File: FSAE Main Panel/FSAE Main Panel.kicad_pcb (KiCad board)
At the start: 2 copper layers, 175 x 58.5 mm, 150 parts, among them J201 USB Micro B, J202 Cortex_Debug, J203 Conn_01x04, J204 TE_84953-6_FPC, Q301 IRLML6402TRPBF, Q501 SI2308CDS-T1-GE3, Q502 SI2308CDS-T1-GE3, SW1 B3W-1020, SW2 B3W-1020, U1 SAMD21G18A-AU, U301 UA7805CKTTR, U302 LP2985-3.3, U303 LM1085-5.0, U304 UA7805CKTTR, U401 MCP2515-I/ST, U402 MCP2551-I/SN, U501 TLC6C598, U502 TLC6C5816, U503 TLC6C5816, U504 TLC6C5816, Y101 32.768kHz, Y401 Resonator

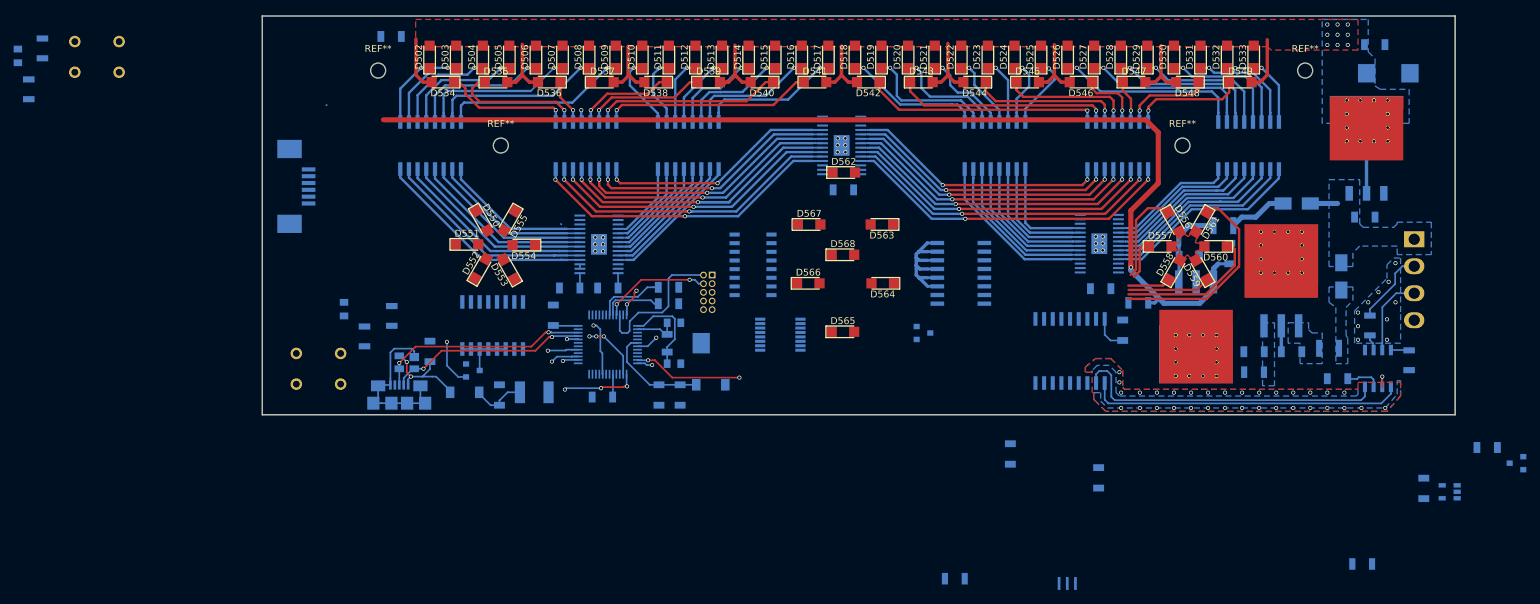
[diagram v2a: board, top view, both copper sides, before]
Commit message: Power Supply Changes Again
Shrunk some 5V layout by switching LM7805's for their SOT223 packages but with very careful top copper considerations for thermal management.
Shrunk the Right side by 12mm for more clearance near ignition button.
Fixed Shift Register clock signal routing.
Changed shift order to be 7 segment first for easiler routing.
Added Mounting Holes.
TODO: Figure out Top layer 7 segment placement.
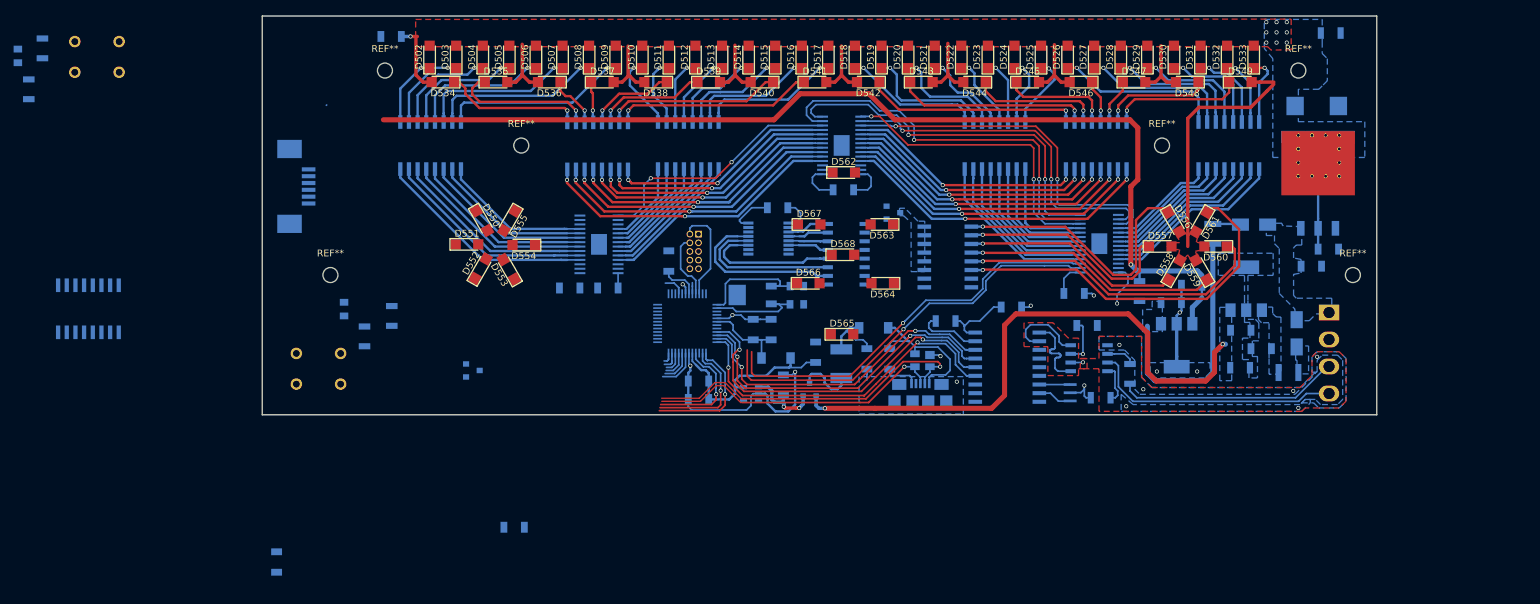
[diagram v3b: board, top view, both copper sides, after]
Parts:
- added REF**: MountingHole_2.2mm_M2, Mounting_Holes:MountingHole_2.2mm_M2, F.Cu at (87.5, 68.0)
- added REF**: MountingHole_2.2mm_M2, Mounting_Holes:MountingHole_2.2mm_M2, F.Cu at (237.5, 68.0)
- U301, U304: value UA7805CKTTR -> LM7805; footprint Texas_Additions:TO-263-3_TabPin2_PAD_2012 -> TO_SOT_Packages_SMD:SOT-223-3_TabPin2
- moved C305 107.2 mm to (141.5, 86.2), turned to 180 degrees
- moved Q301 104.3 mm to (157.8, 84.8), turned to 90 degrees
- moved C304 103.7 mm to (153.9, 84.2), turned to 90 degrees
- moved U302 103.5 mm to (149.2, 85.4)
- moved R302 78.0 mm to (234.2, 32.5)
- moved J201 76.5 mm to (174.1, 86.6)
- moved D201 75.7 mm to (174.3, 80.5)
- moved C203 67.5 mm to (169.6, 80.3), turned to 90 degrees
- moved L201 60.7 mm to (167.2, 75.8), turned to 0 degrees
- moved RN508 59.4 mm to (52.0, 73.0)
- moved C106 54.4 mm to (79.6, 110.1)
- moved C204 54.2 mm to (166.2, 80.3), turned to 90 degrees
- moved C502 49.7 mm to (153.1, 58.1), turned to 180 degrees
- moved R402 45.6 mm to (200.5, 86.0), turned to 180 degrees
- moved C501 45.4 mm to (158.7, 79.3), turned to 90 degrees
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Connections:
- J203 pad 2: CAN_IN- -> GND
- J203 pad 3: CAN_IN+ -> CAN_IN-
- J203 pad 4: GND -> CAN_IN+
- RN501 pad 1: /Display/aI -> /Display/a
- RN501 pad 10: /Display/g -> /Display/gI
- RN501 pad 11: /Display/f -> /Display/fI
- RN501 pad 12: /Display/e -> /Display/eI
- RN501 pad 13: /Display/d -> /Display/dI
- RN501 pad 14: /Display/c -> /Display/cI
- RN501 pad 15: /Display/b -> /Display/bI
- RN501 pad 16: /Display/a -> /Display/aI
- RN501 pad 2: /Display/bI -> /Display/b
- RN501 pad 3: /Display/cI -> /Display/c
- RN501 pad 4: /Display/dI -> /Display/d
- RN501 pad 5: /Display/eI -> /Display/e
- RN501 pad 6: /Display/fI -> /Display/f
- RN501 pad 7: /Display/gI -> /Display/g
- U1 pad 20: RPM_IN -> GEAR_IN
- U1 pad 24: RPM_SCLK -> SCLK
- U1 pad 30: GEAR_SCLK -> Net-(U1-Pad30)
- U501 pad 15: GEAR_SCLK -> SCLK
- U501 pad 9: Net-(U501-Pad9) -> GEAR_OUT
- U502 pad 12: RPM_IN -> GEAR_OUT
- U502 pad 17: RPM_SCLK -> SCLK
- U503 pad 12: Net-(U502-Pad15) -> Net-(U503-Pad12)
- U503 pad 17: RPM_SCLK -> SCLK
- U504 pad 12: Net-(U503-Pad15) -> Net-(U502-Pad15)
- U504 pad 15: GEAR_IN -> Net-(U503-Pad12)
- U504 pad 17: RPM_SCLK -> SCLK
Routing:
- net +5V: track 0.00 -> 96.1 mm, vias 0 -> 4
- net GND: track 33.6 -> 96.3 mm, vias 43 -> 20
- net RPM_CLR: track 0.00 -> 61.6 mm, vias 0 -> 2
- net /Display/~G3: track 0.00 -> 60.8 mm, vias 0 -> 1
- net /Display/~G4: track 0.00 -> 59.3 mm, vias 0 -> 1
- net ~RPM_EN: track 0.00 -> 59.0 mm, vias 0 -> 2
- net RPM_RCLK: track 0.00 -> 55.3 mm, vias 0 -> 2
- net SCLK: track 0.00 -> 55.1 mm, vias 0 -> 2
- net CAN_MOSI: track 0.00 -> 52.2 mm, vias 0 -> 2
- net CAN_MISO: track 0.00 -> 49.2 mm, vias 0 -> 2
- net CAN_SCLK: track 2.25 -> 50.5 mm, vias 1 -> 2
- net Net-(U503-Pad12): track 0.00 -> 44.3 mm, vias 0 -> 2
- net Net-(U502-Pad15): track 0.00 -> 37.2 mm, vias 0 -> 2
- net +3V3: track 28.5 -> 65.1 mm, vias 0 -> 1
- net /CAN/CAN_TX+: track 46.3 -> 12.0 mm
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- added copper zone on B.Cu, net /Display/OP_CONTROL
- added copper zone on B.Cu, net /Power/REG2_VIN
- removed copper zone on F.Cu, net DWC_+5V
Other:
- board size 175 x 58.5 mm -> 163.5 x 58.5 mm
- board text removed: "Maximum length 160mm"
- board text removed: "Maximum width 55mm"

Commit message: Minor Routing changes
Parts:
- moved SW2 6.52 mm to (89.0, 84.5)
- moved C504 4.72 mm to (123.5, 70.3)
- moved C503 4.21 mm to (122.9, 74.1)
- moved C402 3.95 mm to (183.7, 74.0)
- moved U502 3.30 mm to (123.6, 63.5)
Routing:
- net +3V3: track 65.1 -> 116.7 mm, vias 1 -> 3
- net GND: track 96.3 -> 128.1 mm, vias 20 -> 27
- net /Display/RPM_10: track 13.2 -> 16.7 mm
- net /Display/RPM_3: track 29.6 -> 26.3 mm
- net /Display/RPM_8: track 22.1 -> 18.8 mm
- net /Display/RPM_7: track 23.4 -> 20.1 mm
- net /Display/RPM_6: track 24.9 -> 21.6 mm
- net /Display/RPM_5: track 26.5 -> 23.2 mm
- net /Display/RPM_4: track 28.0 -> 24.7 mm
- net /Display/RPM_1: track 32.6 -> 29.3 mm
- net /Display/RPM_2: track 31.1 -> 27.8 mm
- net /Display/RPM_12: track 15.9 -> 19.2 mm
- net /Display/RPM_9: track 11.9 -> 15.2 mm
- net /Display/RPM_16: track 20.8 -> 24.1 mm
- net /Display/RPM_15: track 19.5 -> 22.8 mm
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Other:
- board size 163.5 x 58.5 mm -> 157 x 58.5 mm

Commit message: More Routing
Fixed Tactile Switch Footprints
More routing
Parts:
- moved C201 69.7 mm to (103.7, 67.7), turned to 0 degrees
- moved R201 67.7 mm to (103.8, 71.0), turned to 180 degrees
- moved R202 64.2 mm to (98.2, 71.0), turned to 180 degrees
- moved C106 63.7 mm to (131.2, 72.8), turned to 270 degrees
- moved RN508 61.2 mm to (113.1, 76.7)
- moved SW1 55.3 mm to (99.5, 63.0), turned to 180 degrees
- moved C107 45.3 mm to (137.4, 65.9), turned to 90 degrees
- moved C202 14.5 mm to (103.6, 76.5), turned to 0 degrees
- moved C105 10.9 mm to (145.1, 68.8), turned to 0 degrees
- moved Q501 10.3 mm to (118.6, 83.5), turned to 180 degrees
- moved J204 10.0 mm to (90.5, 49.0)
- moved R203 7.25 mm to (103.8, 74.0), turned to 180 degrees
- moved R204 6.42 mm to (98.2, 74.0), turned to 180 degrees
- moved C104 5.74 mm to (150.2, 73.2)
- moved SW2 4.67 mm to (93.0, 82.0)
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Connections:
- C104 pad 2: /XOUT -> /XIN-
- C105 pad 2: /XIN -> /XIN+
- SW1 pad 2: /External Interface/SW1_L -> GND
- SW1 pad 3: (no net) -> /External Interface/SW1_L
- SW1 pad 4: (no net) -> /External Interface/SW1_L
- SW2 pad 2: /External Interface/SW2_L -> GND
- SW2 pad 3: (no net) -> /External Interface/SW2_L
- SW2 pad 4: (no net) -> /External Interface/SW2_L
- U1 pad 1: /XIN -> /XIN+
- U1 pad 2: /XOUT -> /XIN-
- Y101 pad 1: /XOUT -> /XIN+
- Y101 pad 2: /XIN -> /XIN-
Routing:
- net DWC_SCLK: track 18.3 -> 116.8 mm, vias 1 -> 2
- net DWC_SDI: track 19.3 -> 117.1 mm, vias 1 -> 2
- net ~CHECK_ENGINE: track 0.00 -> 91.2 mm, vias 0 -> 2
- net ~RESET: track 3.21 -> 70.2 mm, vias 0 -> 1
- net ~CLEAR: track 17.0 -> 48.3 mm, vias 1 -> 2
- net +3V3: track 116.7 -> 143.6 mm
- net /Display/HT6: track 0.00 -> 21.4 mm, vias 0 -> 1
- net /Display/HT1: track 0.00 -> 21.2 mm, vias 0 -> 1
- net /XIN: track 17.2 -> 0.00 mm
- net /XOUT: track 14.6 -> 0.00 mm
- net /External Interface/SW2_L: track 0.00 -> 12.8 mm
- net /External Interface/SW1_L: track 0.00 -> 12.8 mm
- net /Display/HT2: track 0.00 -> 11.5 mm, vias 0 -> 1
- net /Display/HT5: track 0.00 -> 11.2 mm, vias 0 -> 1
- net /XIN-: track 0.00 -> 8.47 mm
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- added copper zone on B.Cu, net /Display/HT_CONTROL

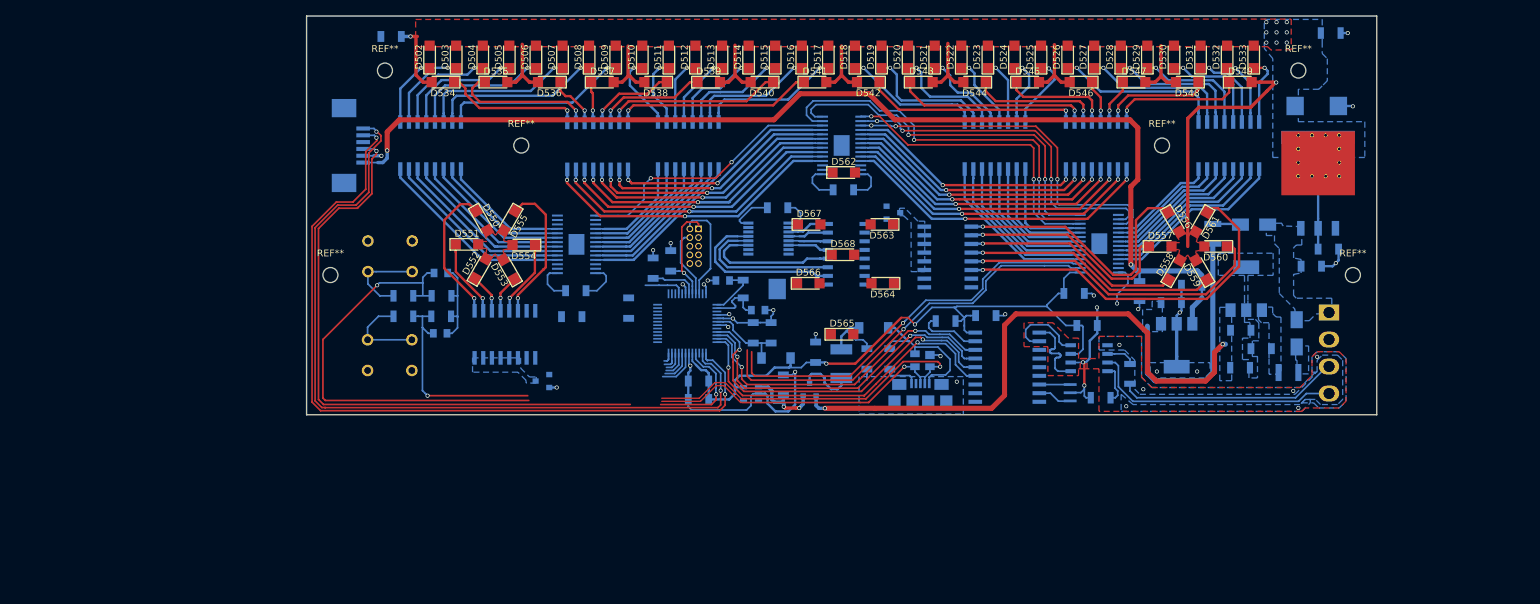
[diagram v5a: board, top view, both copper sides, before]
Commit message: Most Signal Routing
Todo: Figure out 7 segment LED placements and route their power traces
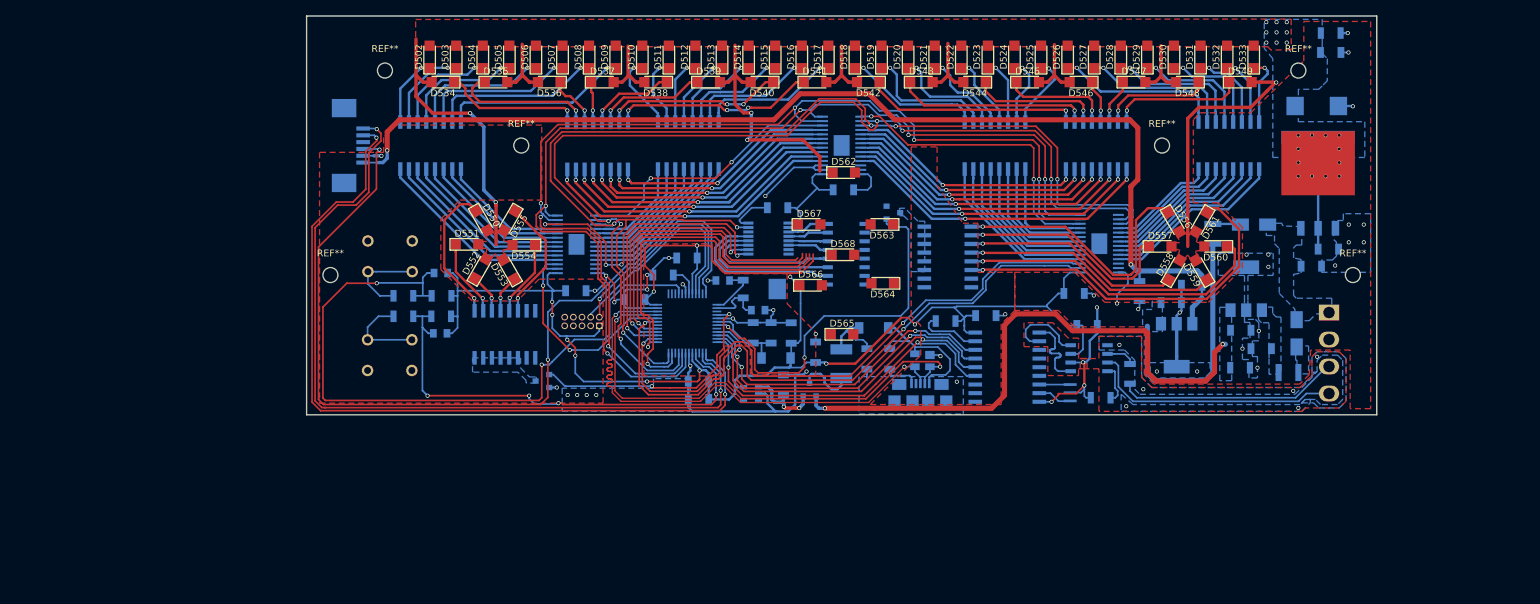
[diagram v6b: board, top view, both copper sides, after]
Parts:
- moved C507 137.9 mm to (234.2, 35.4), turned to 180 degrees
- moved C503 32.3 mm to (155.1, 76.5), turned to 270 degrees
- moved J202 20.3 mm to (127.0, 75.5), turned to 90 degrees
- moved C107 2.42 mm to (139.8, 65.5), turned to 180 degrees
- moved C108 1.78 mm to (136.3, 68.0), turned to 180 degrees
- moved C106 1.54 mm to (132.2, 71.6), turned to 180 degrees
- moved D566 0.45 mm to (157.9, 69.5)
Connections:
- net /Display/~G3 renamed /Display/~PWM_YELLOW
- net /~G3 renamed /~PWM_YELLOW
- net GEAR_RCLK renamed GEAR_SET
- net SCLK renamed FRAME_CLK
- net ~GEAR_PWM renamed ~PWM_WHITE
- U1 pad 19: GEAR_IN -> ~RPM_EN
- U1 pad 20: GEAR_IN -> RPM_CLR
- U1 pad 21: ~RPM_EN -> RPM_SET
- U1 pad 22: RPM_CLR -> Net-(U1-Pad22)
- U1 pad 23: RPM_RCLK -> FRAME_IN
- U1 pad 25: /~G5 -> /Display/~PWM_BLUE
- U1 pad 26: /~G4 -> /Display/~PWM_RED
- U1 pad 32: /~G1 -> /Display/~PWM_GREEN
- U501 pad 2: GEAR_IN -> FRAME_IN
- U502 pad 16: RPM_RCLK -> RPM_SET
- U502 pad 2: /Display/~G1 -> /Display/~PWM_GREEN
- U502 pad 3: /Display/~G2 -> /Display/~PWM_GREEN
- U503 pad 16: RPM_RCLK -> RPM_SET
- U503 pad 3: /Display/~G4 -> /Display/~PWM_RED
- U504 pad 16: RPM_RCLK -> RPM_SET
- U504 pad 2: /Display/~G5 -> /Display/~PWM_BLUE
- U504 pad 3: /Display/~G6 -> /Display/~PWM_BLUE
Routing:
- net RPM_SET: track 0.00 -> 156.7 mm, vias 0 -> 6
- net FRAME_CLK: track 55.1 -> 174.2 mm, vias 3 -> 6
- net +3V3: track 143.6 -> 248.1 mm, vias 3 -> 11
- net ~RPM_EN: track 59.0 -> 154.3 mm, vias 2 -> 5
- net RPM_CLR: track 61.6 -> 156.8 mm, vias 2 -> 6
- net /Display/~PWM_RED: track 0.00 -> 89.2 mm, vias 0 -> 2
- net /Display/~PWM_BLUE: track 0.00 -> 59.8 mm, vias 0 -> 2
- net /Display/~G4: track 59.3 -> 0.00 mm, vias 1 -> 0
- net LED_+5V: track 130.3 -> 186.1 mm, vias 11 -> 14
- net RPM_RCLK: track 55.3 -> 0.00 mm, vias 3 -> 0
- net FRAME_IN: track 0.00 -> 54.4 mm, vias 0 -> 1
- net OIL_PRES: track 1.76 -> 55.2 mm, vias 1 -> 2
- net ~PWM_WHITE: track 0.00 -> 45.2 mm, vias 0 -> 1
- net GEAR_CLR: track 0.00 -> 45.0 mm, vias 0 -> 1
- net GEAR_OUT: track 0.00 -> 44.6 mm, vias 0 -> 4
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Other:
- net class Tiny: via_dia 0.4 -> 0.5

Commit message: Version 1
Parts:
- moved C101 2.90 mm to (149.2, 76.5)
- moved C102 2.47 mm to (152.0, 76.5)
- moved D564 2.32 mm to (168.1, 71.5)
- moved D562 2.22 mm to (163.9, 54.9), turned to 180 degrees
- moved D565 1.61 mm to (161.0, 76.3)
- moved D566 1.59 mm to (156.9, 70.7)
- moved D567 0.85 mm to (156.9, 60.2)
- moved D568 0.51 mm to (162.5, 65.5), turned to 180 degrees
- moved D563 0.48 mm to (168.1, 60.2)
- renumbered REF** to M2
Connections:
- net /Display/~PWM_BLUE renamed ~PWM_BLUE
- net /Display/~PWM_GREEN renamed ~PWM_GREEN
- net /Display/~PWM_RED renamed ~PWM_RED
- D562 pad 2: LED_5V+ -> LED_+5V
- D563 pad 2: LED_5V+ -> LED_+5V
- D564 pad 2: LED_5V+ -> LED_+5V
- D565 pad 2: LED_5V+ -> LED_+5V
- D566 pad 2: LED_5V+ -> LED_+5V
- D567 pad 2: LED_5V+ -> LED_+5V
- D568 pad 2: LED_5V+ -> LED_+5V
- U1 pad 31: /~PWM_YELLOW -> ~PWM_YELLOW
- U502 pad : (no net) -> HEAT1
- U503 pad : (no net) -> HEAT3
- U503 pad 2: /Display/~PWM_YELLOW -> ~PWM_YELLOW
- U504 pad : (no net) -> HEAT2
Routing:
- net ~PWM_YELLOW: track 0.00 -> 93.2 mm, vias 0 -> 2
- net /Display/~PWM_YELLOW: track 93.2 -> 0.00 mm, vias 2 -> 0
- net /Display/f: track 0.00 -> 46.2 mm, vias 0 -> 1
- net +3V3: track 248.1 -> 205.3 mm, vias 11 -> 12
- net GND: track 164.7 -> 193.9 mm, vias 52 -> 62
- net /Display/e: track 0.00 -> 29.0 mm, vias 0 -> 1
- net /Display/d: track 0.00 -> 28.4 mm, vias 0 -> 1
- net FRAME_IN: track 54.4 -> 76.6 mm, vias 1 -> 2
- net /Display/c: track 0.00 -> 15.0 mm, vias 0 -> 1
- net ~PWM_BLUE: track 59.8 -> 73.3 mm
- net LED_+5V: track 186.1 -> 177.3 mm
- net /Display/a: track 0.00 -> 8.41 mm, vias 0 -> 1
- net /Display/b: track 0.00 -> 8.32 mm, vias 0 -> 1
- net /Display/g: track 0.00 -> 7.74 mm, vias 0 -> 1
- net +5V: track 96.1 -> 99.9 mm
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- added copper zone on B.Cu, net +3V3
- added copper zone on B.Cu, net DWC_+5V
- added copper zone on F.Cu, net HEAT1
- added copper zone on F.Cu, net HEAT2
- added copper zone on F.Cu, net HEAT3
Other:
- net class Tiny removed
- net class Wide removed
- rule trace_min: 0.175 -> 0.2
- board text added: "+5V, Reg thermal Pad"
- board text added: "10"
- board text added: "100"
- board text added: "105"
- board text added: "110"
- board text added: "115"
- board text added: "120"
- board text added: "125"
- board text added: "130"
- board text added: "135"
- board text added: "140"
- board text added: "145"
- board text added: "15"
- board text added: "150"
- board text added: "20"
- board text added: "25"
- board text added: "30"
- board text added: "35"
- board text added: "40"
- board text added: "45"
- board text added: "5"
- board text added: "50"
- board text added: "55"
- board text added: "60"
- board text added: "65"
- board text added: "70"
- board text added: "75"
- board text added: "80"
- board text added: "85"
- board text added: "90"
- board text added: "95"
- board text added: ": RPM x 100"
- board text added: "Alex Podgorski Gary Chow Matt Cox"
- board text added: "BLUE (16)"
- board text added: "CAN+"
- board text added: "CAN-"
- board text added: "Designed by:"
- board text added: "ERR"
- board text added: "GEAR POSITION"
- board text added: "GND"
- board text added: "GREEN (16)"
- board text added: "High Temperature Warning"
- board text added: "J203"
- board text added: "Low Oil Pressure Warning"
- board text added: "RED"
- board text added: "REV 1 3-16-19 A.P."
- board text added: "RPM x 100 :"
- board text added: "S1"
- board text added: "S2"
- board text added: "S3"
- board text added: "SHIFT"
- board text added: "UCONN FORMULA SAE 2019"
- board text added: "VBAT"
- board text added: "YELLOW"
- board text added: "a"
- board text added: "b"
- board text added: "c"
- board text added: "d"
- board text added: "e"
- board text added: "f"
- board text added: "g"
